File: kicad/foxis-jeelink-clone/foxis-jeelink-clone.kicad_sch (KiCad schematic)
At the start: 27 parts, among them J1 USB_A, J2 AVR-ISP-6, J3 SMA connector, J4 WireAntenna, U1 ATmega328P-A, U2 FT232RL, U3 RFM69CW, X1 16 MHz

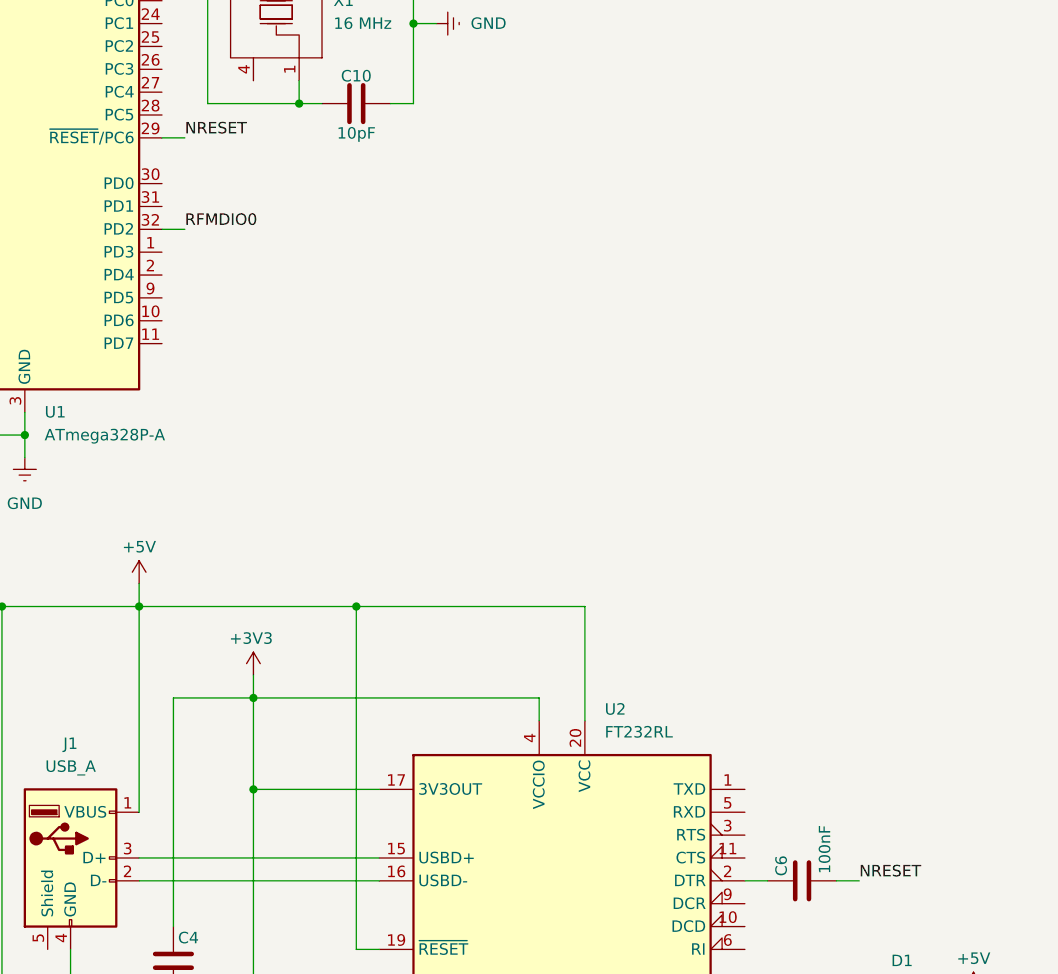
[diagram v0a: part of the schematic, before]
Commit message: fix massive error that made Rev. 0 completely nonfunctional. I simply forgot to connect RX and TX. Absolutely no idea how I managed to mess this up.
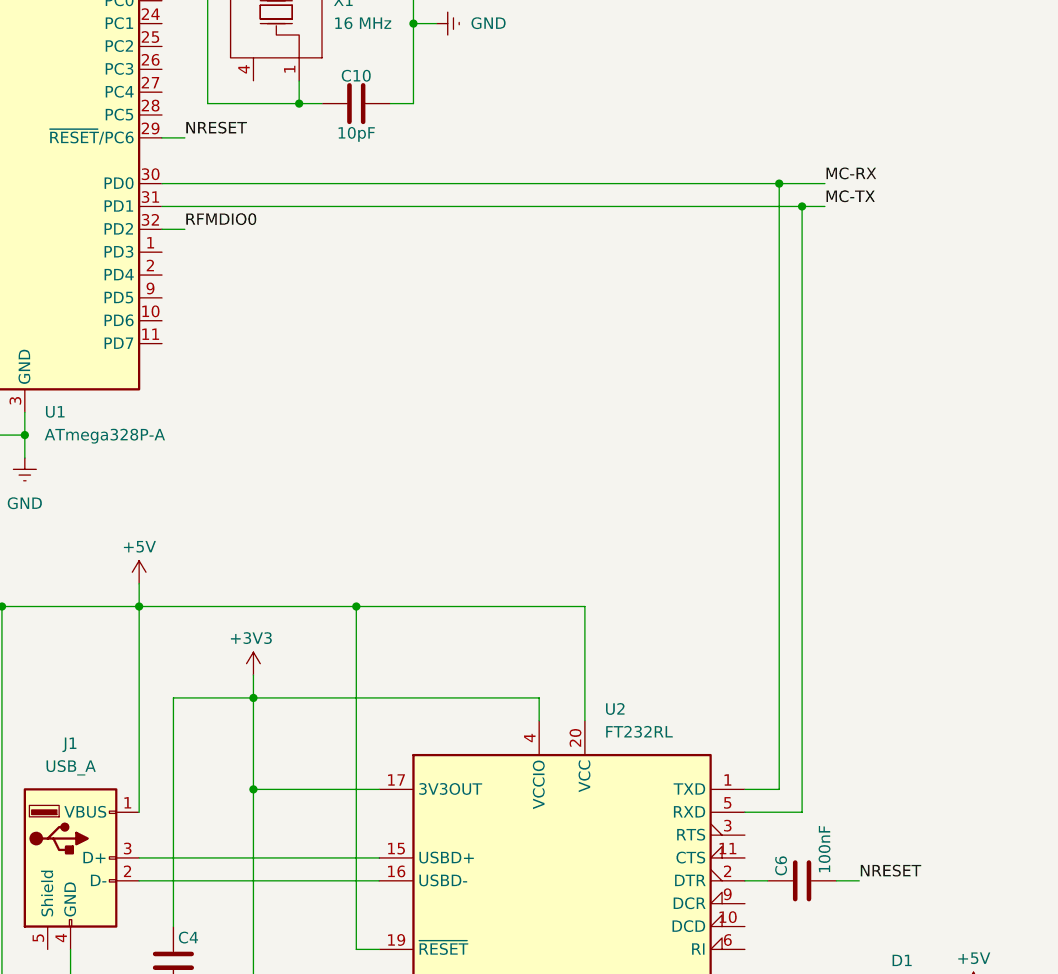
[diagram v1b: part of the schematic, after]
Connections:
- net MC-RX: now reaches U2.1 (TXD)
- net MC-RX: now also U1.30 (PD0)
- net MC-TX: now reaches U2.5 (RXD)
- net MC-TX: now also U1.31 (PD1)
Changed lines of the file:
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@@
+	)
+	(junction
+		(at 121.92 73.66)
+		(diameter 0)
+		(color 0 0 0 0)
 	)
 	(junction
@@
 	)
 	(junction
+		(at 124.46 76.2)
+		(diameter 0)
+		(color 0 0 0 0)
+	)
+	(junction
 		(at 215.9 74.93)
 		(diameter 0)
@@
 	(wire
 		(pts
+			(xy 121.92 140.97) (xy 121.92 73.66)
+		)
+		(stroke
+			(width 0)
+			(type default)
+		)
+	)
+	(wire
+		(pts
 			(xy 40.64 20.32) (xy 45.72 20.32)
 		)
@@
 	(wire
 		(pts
+			(xy 121.92 73.66) (xy 53.34 73.66)
+		)
+		(stroke
+			(width 0)
+			(type default)
+		)
+	)
+	(wire
+		(pts
 			(xy 68.58 64.77) (xy 71.12 64.77)
 		)
@@
 	(wire
 		(pts
+			(xy 124.46 143.51) (xy 124.46 76.2)
+		)
+		(stroke
+			(width 0)
+			(type default)
+		)
+	)
+	(wire
+		(pts
 			(xy 205.74 69.85) (xy 205.74 77.47)
 		)
@@
 	(wire
 		(pts
+			(xy 118.11 140.97) (xy 121.92 140.97)
+		)
+		(stroke
+			(width 0)
+			(type default)
+		)
+	)
+	(wire
+		(pts
 			(xy 97.79 186.69) (xy 92.71 186.69)
 		)
@@
 	(wire
 		(pts
+			(xy 121.92 73.66) (xy 127 73.66)
+		)
+		(stroke
+			(width 0)
+			(type default)
+		)
+	)
+	(wire
+		(pts
 			(xy 118.11 151.13) (xy 120.65 151.13)
 		)
@@
 	(wire
 		(pts
+			(xy 124.46 76.2) (xy 53.34 76.2)
+		)
+		(stroke
+			(width 0)
+			(type default)
+		)
+	)
+	(wire
+		(pts
 			(xy 21.59 120.65) (xy 29.21 120.65)
 		)
@@
 	(wire
 		(pts
+			(xy 118.11 143.51) (xy 124.46 143.51)
+		)
+		(stroke
+			(width 0)
+			(type default)
+		)
+	)
+	(wire
+		(pts
 			(xy 68.58 33.02) (xy 71.12 33.02)
 		)
@@
 		(pts
 			(xy 38.1 99.06) (xy 38.1 101.6)
+		)
+		(stroke
+			(width 0)
+			(type default)
+		)
+	)
+	(wire
+		(pts
+			(xy 124.46 76.2) (xy 127 76.2)
 		)
 		(stroke
@@
 		)
 	)
+	(label "MC-RX"
+		(at 127 73.66 0)
+		(fields_autoplaced yes)
+		(effects
+			(font
+				(size 1.27 1.27)
+			)
+			(justify left bottom)
+		)
+	)
 	(label "NSS"
 		(at 215.9 92.71 180)
@@
 		(fields_autoplaced yes)
 		(effects
+			(font
+				(size 1.27 1.27)
+			)
+			(justify left bottom)
+		)
+	)
+	(label "MC-TX"
+		(at 127 76.2 0)
+		(fields_autoplaced yes)
+		(effects

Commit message: rev. 1 as sent to JLCPCB
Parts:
- added C12: 22uF, Capacitor_SMD:C_0603_1608Metric, symbol Device:C
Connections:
- net +3V3: now also C12.1
- net GND: now also C12.2
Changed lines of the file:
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@@
+	(wire
+		(pts
+			(xy 204.47 128.27) (xy 204.47 129.54)
+		)
+		(stroke
+			(width 0)
+			(type default)
+		)
+	)
 	(wire
 		(pts
@@
 		(pts
 			(xy 81.28 33.02) (xy 78.74 33.02)
+		)
+		(stroke
+			(width 0)
+			(type default)
+		)
+	)
+	(wire
+		(pts
+			(xy 204.47 119.38) (xy 204.47 120.65)
 		)
 		(stroke
@@
 	)
 	(symbol
+		(lib_id "power:Earth")
+		(at 204.47 129.54 0)
+		(unit 1)
+		(exclude_from_sim no)
+		(in_bom yes)
+		(on_board yes)
+		(dnp no)
+		(fields_autoplaced yes)
+		(property "Reference" "#PWR016"
+			(at 204.47 135.89 0)
+			(effects
+				(font
+					(size 1.27 1.27)
+				)
+				(hide yes)
+			)
+		)
+		(property "Value" "GND"
+			(at 204.47 134.62 0)
+			(effects
+				(font
+					(size 1.27 1.27)
+				)
+			)
+		)
+		(property "Footprint" ""
+			(at 204.47 129.54 0)
+			(effects
+				(font
+					(size 1.27 1.27)
+				)
+				(hide yes)
+			)
+		)
+		(property "Datasheet" "~"
+			(at 204.47 129.54 0)
+			(effects
+				(font
+					(size 1.27 1.27)
+				)
+				(hide yes)
+			)
+		)
+		(property "Description" ""
+			(at 204.47 129.54 0)
+			(effects
+				(font
+					(size 1.27 1.27)
+				)
+				(hide yes)
+			)
+		)
+		(pin "1"
+		)
+		(instances
+			(project "foxis-jeelink-clone"
+				(path "/125d9b9f-90a8-43ae-9a7c-df8b27c5127d"
+					(reference "#PWR016")
+					(unit 1)
+				)
+			)
+		)
+	)
+	(symbol
 		(lib_id "Device:C")
 		(at 63.5 168.91 0)
@@
 	(symbol
 		(lib_id "Device:C")
+		(at 204.47 124.46 0)
+		(unit 1)
+		(exclude_from_sim no)
+		(in_bom yes)
+		(on_board yes)
+		(dnp no)
+		(property "Reference" "C12"
+			(at 205.486 121.92 0)
+			(effects
+				(font
+					(size 1.27 1.27)
+				)
+				(justify left)
+			)
+		)
+		(property "Value" "22uF"
+			(at 205.232 127 0)
+			(effects
+				(font
+					(size 1.27 1.27)
+				)
+				(justify left)
+			)
+		)
+		(property "Footprint" "Capacitor_SMD:C_0603_1608Metric"
+			(at 205.4352 128.27 0)
+			(effects
+				(font
+					(size 1.27 1.27)
+				)
+				(hide yes)
+			)
+		)
+		(property "Datasheet" "~"
+			(at 204.47 124.46 0)
+			(effects
+				(font
+					(size 1.27 1.27)
+				)
+				(hide yes)
+			)
+		)
+		(property "Description" "Unpolarized capacitor"
+			(at 204.47 124.46 0)
+			(effects
+				(font
+					(size 1.27 1.27)
+				)
+				(hide yes)
+			)
+		)
+		(pin "1"
+		)
+		(pin "2"
+		)
+		(instances
+			(project "foxis-jeelink-clone"
+				(path "/125d9b9f-90a8-43ae-9a7c-df8b27c5127d"
+					(reference "C12")
+					(unit 1)
+				)
+			)
+		)
+	)
+	(symbol
+		(lib_id "Device:C")
 		(at 74.93 45.72 90)
 		(unit 1)
@@
 					(unit 1)
 				)
+			)
+		)
+	)
+	(symbol
+		(lib_id "power:+3V3")
+		(at 204.47 119.38 0)
+		(unit 1)
+		(exclude_from_sim no)
+		(in_bom yes)
+		(on_board yes)
+		(dnp no)
+		(property "Reference" "#PWR015"
+			(at 204.47 123.19 0)
+			(effects
+				(font
+					(size 1.27 1.27)
+				)
+				(hide yes)
+			)
+		)
+		(property "Value" "+3V3"
+			(at 204.216 115.316 0)
+			(effects
+				(font
+					(size 1.27 1.27)
+				)
+			)
+		)
+		(property "Footprint" ""
+			(at 204.47 119.38 0)
+			(effects
+				(font
+					(size 1.27 1.27)
+				)
+				(hide yes)
+			)
+		)
+		(property "Datasheet" ""
+			(at 204.47 119.38 0)
+			(effects
+				(font
+					(size 1.27 1.27)
+				)
+				(hide yes)
+			)
+		)
+		(property "Description" "Power symbol creates a global label with name \"+3V3\""
+			(at 204.47 119.38 0)
+			(effects
+				(font
+					(size 1.27 1.27)
+				)
+				(hide yes)
+			)
+		)
+		(pin "1"
+		)
+		(instances
+			(project "foxis-jeelink-clone"
+				(path "/125d9b9f-90a8-43ae-9a7c-df8b27c5127d"
+					(reference "#PWR015")
+					(unit 1)
+				)
